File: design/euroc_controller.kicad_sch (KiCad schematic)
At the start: 65 parts, among them J1 xt30, J2 jst_sh 4, J4 jst_sh 4, J5 jst_sh 4, J6 SMA, J8 USB_C_Receptacle_USB2.0, J9 jst_sh 4, Q1 MMBT3904, U1 TPSM5601R5, U13 STM32U575CGTx, U2 USBLC6-2SC6, U3 LSM6DSO32, U4 MS5611-01BA, U5 TCAN332, U6 W25Q128JVS, U7 RFM69W, U8 L86, Y1 48MHz

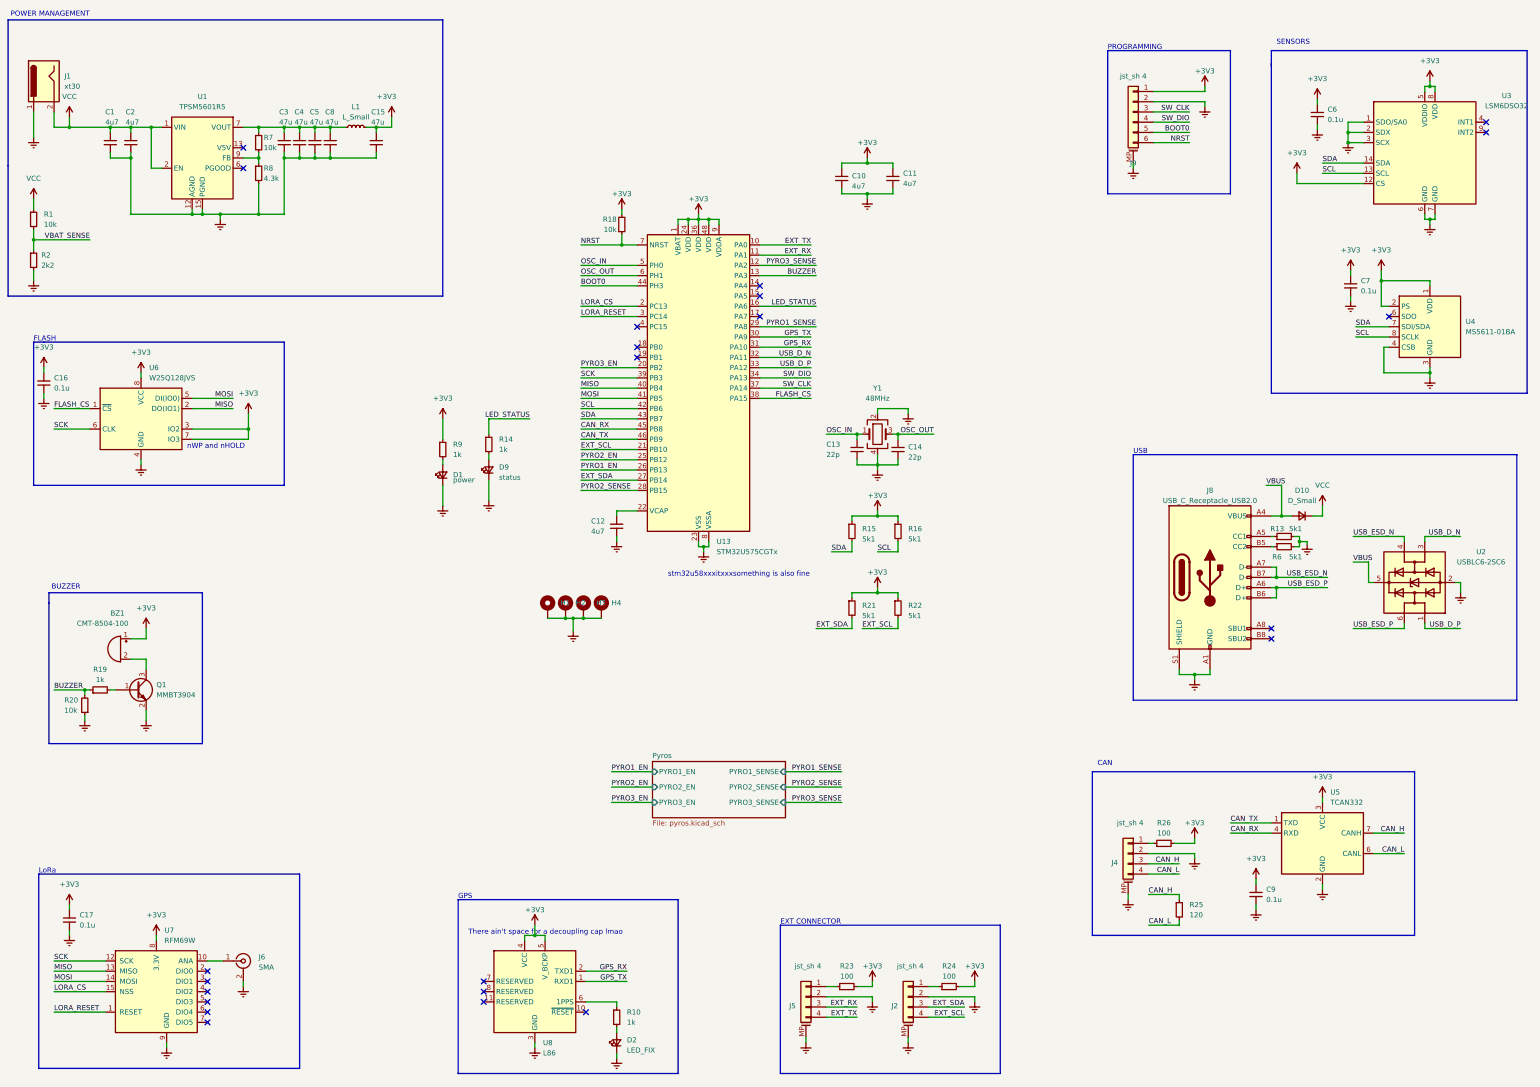
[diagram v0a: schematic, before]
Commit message: route dp
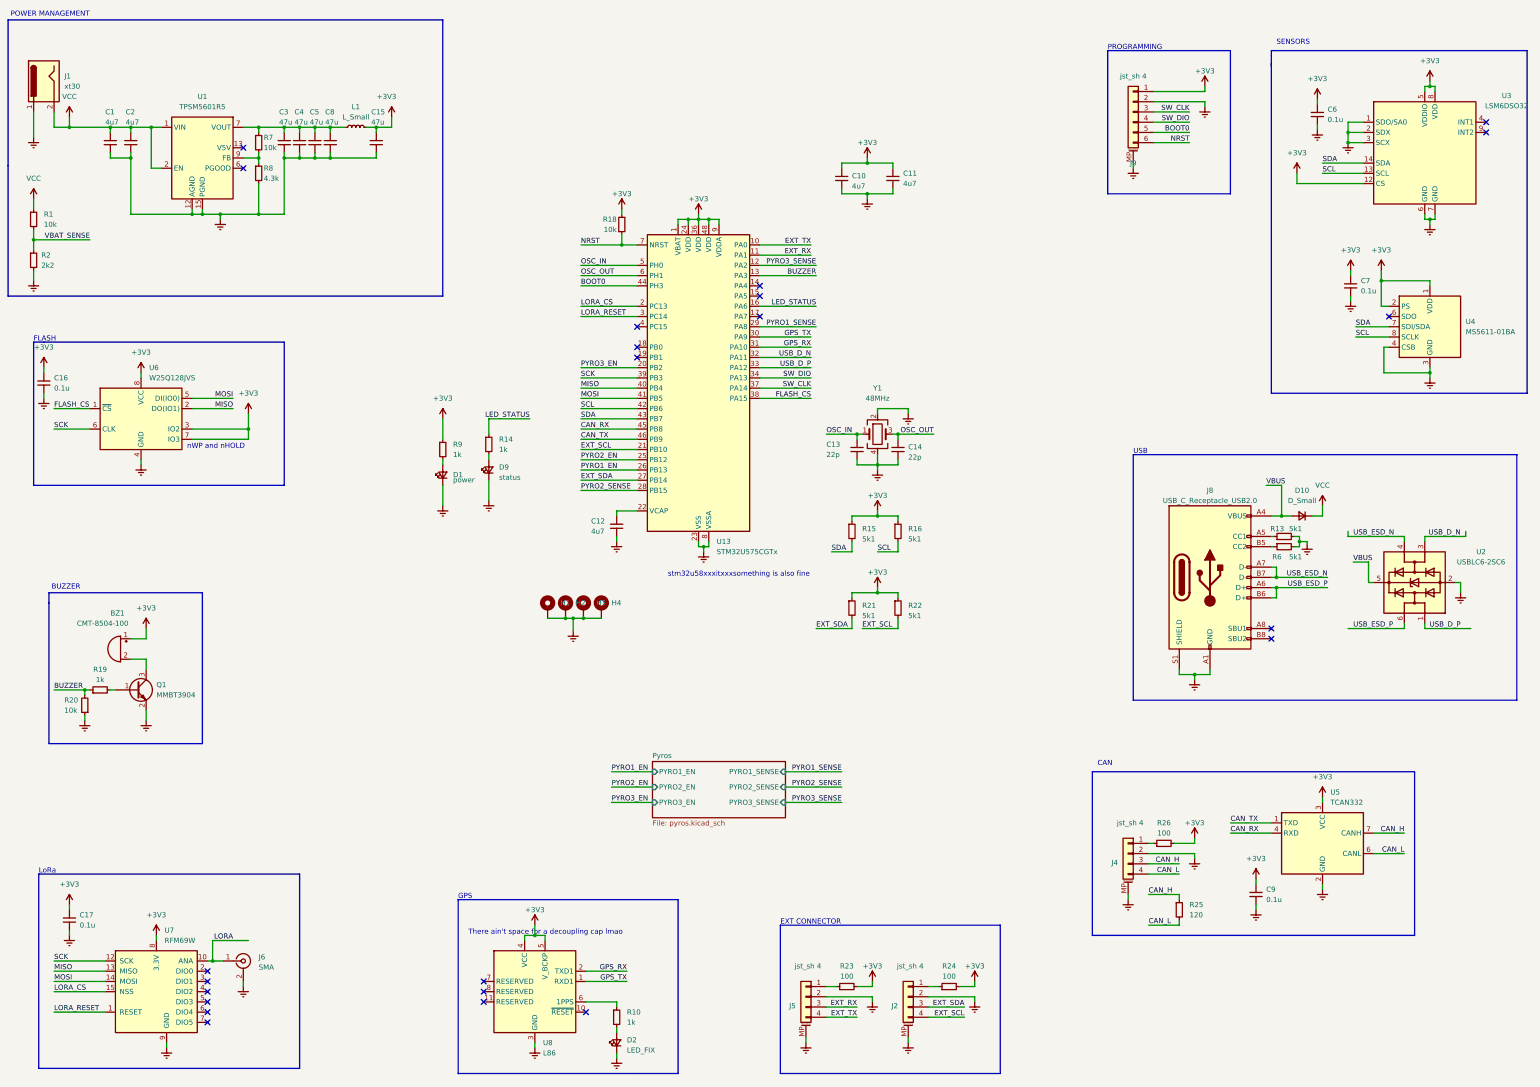
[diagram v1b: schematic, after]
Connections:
- net LORA: now reaches J6.1 (In), U7.10 (ANA)
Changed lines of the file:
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@@
   (junction (at 228.6 158.75) (diameter 0) (color 0 0 0 0)
+  )
+  (junction (at 63.5 250.19) (diameter 0) (color 0 0 0 0)
   )
   (junction (at 65.405 64.77) (diameter 0) (color 0 0 0 0)
@@
     (stroke (width 0) (type default))
   )
-  (wire (pts (xy 364.49 167.64) (xy 373.38 167.64))
-    (stroke (width 0) (type default))
-  )
   (wire (pts (xy 222.25 158.75) (xy 228.6 158.75))
     (stroke (width 0) (type default))
@@
     (stroke (width 0) (type default))
   )
+  (wire (pts (xy 63.5 250.19) (xy 66.04 250.19))
+    (stroke (width 0) (type default))
+  )
   (wire (pts (xy 31.75 182.88) (xy 31.75 184.15))
     (stroke (width 0) (type default))
@@
     (stroke (width 0) (type default))
   )
+  (wire (pts (xy 364.49 167.64) (xy 375.92 167.64))
+    (stroke (width 0) (type default))
+  )
   (wire (pts (xy 326.39 144.78) (xy 327.025 144.78))
     (stroke (width 0) (type default))
@@
     (stroke (width 0) (type default))
   )
+  (wire (pts (xy 374.65 143.51) (xy 374.65 144.78))
+    (stroke (width 0) (type default))
+  )
   (wire (pts (xy 228.6 114.3) (xy 228.6 113.03))
     (stroke (width 0) (type default))
@@
     (stroke (width 0) (type default))
   )
+  (wire (pts (xy 63.5 250.19) (xy 63.5 245.11))
+    (stroke (width 0) (type default))
+  )
   (wire (pts (xy 359.41 144.78) (xy 359.41 146.05))
     (stroke (width 0) (type default))
@@
     (stroke (width 0) (type default))
   )
-  (wire (pts (xy 359.41 144.78) (xy 346.71 144.78))
+  (wire (pts (xy 345.44 144.78) (xy 359.41 144.78))
     (stroke (width 0) (type default))
   )
@@
     (stroke (width 0) (type default))
   )
+  (wire (pts (xy 345.44 143.51) (xy 345.44 144.78))
+    (stroke (width 0) (type default))
+  )
   (wire (pts (xy 322.58 229.87) (xy 322.58 231.14))
     (stroke (width 0) (type default))
@@
     (stroke (width 0) (type default))
   )
+  (wire (pts (xy 345.44 167.64) (xy 359.41 167.64))
+    (stroke (width 0) (type default))
+  )
   (polyline (pts (xy 281.94 203.2) (xy 281.94 243.84))
     (stroke (width 0) (type default))
@@
     (stroke (width 0) (type default))
   )
-  (wire (pts (xy 364.49 144.78) (xy 373.38 144.78))
+  (wire (pts (xy 364.49 144.78) (xy 374.65 144.78))
     (stroke (width 0) (type default))
   )
@@
     (stroke (width 0) (type default))
   )
-  (wire (pts (xy 62.23 250.19) (xy 66.04 250.19))
+  (wire (pts (xy 62.23 250.19) (xy 63.5 250.19))
     (stroke (width 0) (type default))
   )
@@
     (stroke (width 0) (type default))
   )
-  (wire (pts (xy 359.41 167.64) (xy 346.71 167.64))
-    (stroke (width 0) (type default))
-  )
   (wire (pts (xy 309.88 36.83) (xy 309.88 38.1))
     (stroke (width 0) (type default))
@@
     (stroke (width 0) (type default))
   )
+  (wire (pts (xy 63.5 245.11) (xy 72.39 245.11))
+    (stroke (width 0) (type default))
+  )
   (wire (pts (xy 228.6 138.43) (xy 228.6 139.7))
     (stroke (width 0) (type default))
@@
     (effects (font (size 1.27 1.27)) (justify left bottom))
   )
+  (label "LORA" (at 68.58 245.11 180) (fields_autoplaced)
+    (effects (font (size 1.27 1.27)) (justify right bottom))
+  )
   (label "OSC_IN" (at 154.94 77.47 0) (fields_autoplaced)
     (effects (font (size 1.27 1.27)) (justify left bottom))
@@
     (effects (font (size 1.27 1.27)) (justify left bottom))
   )
+  (netclass_flag "" (length 2.54) (shape round) (at 72.39 245.11 0) (fields_autoplaced)
+    (effects (font (size 1.27 1.27)) (justify left bottom))
+    (property "Netclass" "50ohm" (at 73.0885 242.57 0)
+      (effects (font (size 1.27 1.27) italic) (justify left))
+    )
+  )
+  (netclass_flag "" (length 2.54) (shape round) (at 375.92 167.64 180) (fields_autoplaced)
+    (effects (font (size 1.27 1.27)) (justify right bottom))
+    (property "Netclass" "90ohm_d" (at 376.6185 170.18 0)
+      (effects (font (size 1.27 1.27) italic) (justify left))
+    )
+  )
+  (netclass_flag "" (length 2.54) (shape round) (at 374.65 143.51 0) (fields_autoplaced)
+    (effects (font (size 1.27 1.27)) (justify left bottom))
+    (property "Netclass" "90ohm_d" (at 375.3485 140.97 0)
+      (effects (font (size 1.27 1.27) italic) (justify left))
+    )
+  )
+  (netclass_flag "" (length 2.54) (shape round) (at 345.44 167.64 180) (fields_autoplaced)
+    (effects (font (size 1.27 1.27)) (justify right bottom))
+    (property "Netclass" "90ohm_d" (at 346.1385 170.18 0)
+      (effects (font (size 1.27 1.27) italic) (justify left))
+    )
+  )
+  (netclass_flag "" (length 2.54) (shape round) (at 345.44 143.51 0) (fields_autoplaced)
+    (effects (font (size 1.27 1.27)) (justify left bottom))
+    (property "Netclass" "90ohm_d" (at 346.1385 140.97 0)
+      (effects (font (size 1.27 1.27) italic) (justify left))
+    )
+  )
   (symbol (lib_name "Earth_15") (lib_id "power:Earth") (at 226.06 60.96 0) (unit 1)

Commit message: redo for aisler
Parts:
- added R27: 10k, Resistor_SMD:R_0603_1608Metric, symbol Device:R_Small
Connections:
- net BOOT0: now also R27.1
- net Earth: now also R27.2
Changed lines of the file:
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@@
     (stroke (width 0) (type default))
   )
+  (wire (pts (xy 143.51 88.9) (xy 143.51 90.17))
+    (stroke (width 0) (type default))
+  )
   (wire (pts (xy 333.375 146.05) (xy 333.375 144.78))
     (stroke (width 0) (type default))
@@
     (stroke (width 0) (type default))
   )
+  (wire (pts (xy 143.51 82.55) (xy 143.51 83.82))
+    (stroke (width 0) (type default))
+  )
   (wire (pts (xy 186.69 66.04) (xy 186.69 67.31))
     (stroke (width 0) (type default))
@@
     (stroke (width 0) (type default))
   )
-  (wire (pts (xy 154.94 82.55) (xy 168.91 82.55))
+  (wire (pts (xy 143.51 82.55) (xy 168.91 82.55))
     (stroke (width 0) (type default))
   )
@@
     )
   )
+  (symbol (lib_id "Device:R_Small") (at 143.51 86.36 0) (unit 1)
+    (in_bom yes) (on_board yes) (dnp no) (fields_autoplaced)
+    (property "Reference" "R27" (at 146.05 85.09 0)
+      (effects (font (size 1.27 1.27)) (justify left))
+    )
+    (property "Value" "10k" (at 146.05 87.63 0)
+      (effects (font (size 1.27 1.27)) (justify left))
+    )
+    (property "Footprint" "Resistor_SMD:R_0603_1608Metric" (at 143.51 86.36 0)
+      (effects (font (size 1.27 1.27)) hide)
+    )
+    (property "Datasheet" "~" (at 143.51 86.36 0)
+      (effects (font (size 1.27 1.27)) hide)
+    )
+    (pin "1")
+    (pin "2")
+    (instances
+      (project "euroc_controller"
+        (path "/14304acd-da5a-4fe2-9970-30001d32799f"
+          (reference "R27") (unit 1)
+        )
+      )
+    )
+  )
   (symbol (lib_id "power:+3V3") (at 21.59 102.87 0) (unit 1)
     (in_bom yes) (on_board yes) (dnp no)
@@
         )
       )
+    )
+  )
+  (symbol (lib_name "Earth_25") (lib_id "power:Earth") (at 143.51 90.17 0) (unit 1)
+    (in_bom yes) (on_board yes) (dnp no) (fields_autoplaced)
+    (property "Reference" "#PWR059" (at 143.51 96.52 0)
+      (effects (font (size 1.27 1.27)) hide)
+    )
+    (property "Value" "Earth" (at 143.51 93.98 0)
+      (effects (font (size 1.27 1.27)) hide)
+    )
+    (property "Footprint" "" (at 143.51 90.17 0)
+      (effects (font (size 1.27 1.27)) hide)
+    )
+    (property "Datasheet" "~" (at 143.51 90.17 0)
+      (effects (font (size 1.27 1.27)) hide)
+    )
+    (pin "1")
+    (instances
+      (project "euroc_controller"
+        (path "/14304acd-da5a-4fe2-9970-30001d32799f"
+          (reference "#PWR059") (unit 1)
+        )
+      )
